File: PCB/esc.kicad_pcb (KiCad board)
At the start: 4 copper layers, 43.5 x 65 mm, 70 parts, among them J1 Conn_01x04_Pin, J2 Conn_01x01, J3 Conn_01x01, J4 Conn_01x01, J5 Conn_01x01, J6 Conn_01x01, Q1 XRS230N03C, Q2 XRS230N03C, Q3 XRS230N03C, Q4 XRS230N03C, Q5 XRS230N03C, Q6 XRS230N03C, SW1 SW_SPST, U1 STM32C031K6T6, U2 TLV76133DCY, U3 LMV324A, U4 INA180A3, U5 IRS21867S, U6 IRS21867S, U7 IRS21867S

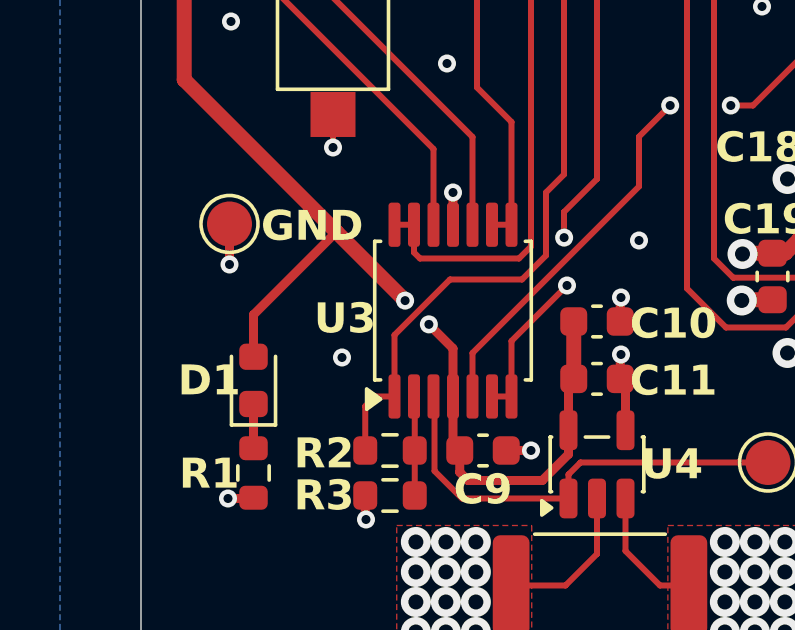
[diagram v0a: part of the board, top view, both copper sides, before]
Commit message: Swapped opamp
Desgin now specifies an opamp with rail-to-rail input.
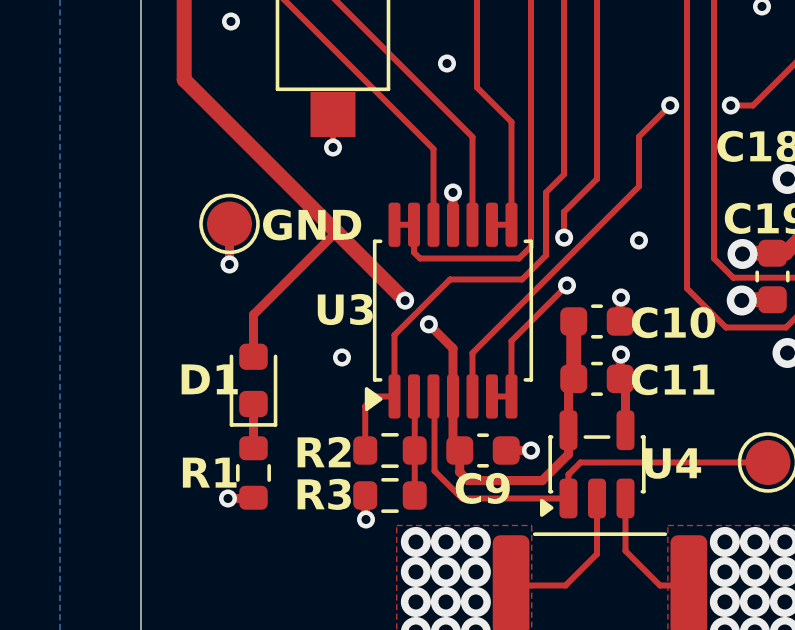
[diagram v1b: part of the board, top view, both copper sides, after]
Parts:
- U3: value LMV324A -> TLV9064
